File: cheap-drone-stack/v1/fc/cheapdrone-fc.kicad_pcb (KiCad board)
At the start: 4 copper layers, 33.8 x 33.8 mm, 77 parts, among them Y1 8MHz

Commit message: Cheap drone stack: OffGrid brand silkscreen on the FC, verification script
- brand.py: Beacon Ring and lockup from the v3.2 hand-off SVG numbers,
  Instrument Sans / JetBrains Mono outlines shaped with HarfBuzz from the
  vendored OFL variable fonts; styles follow tokens.json
- FC: lockup on the bottom, bare mark and pad codes on the top, matte black
  mask / white silk / ENIG written into the board stackup; LED and spare
  GND breakout pads swapped so every label fits at a printable size
- ESC: six layers (In1 GND, In4 VBAT, four signal layers); bottom channels
  trade MCU and BEMF ends so no two QFNs sit back to back (routing WIP)
- verify.py: pin maps against KiCad symbols and the Betaflight/AM32
  sources, power arithmetic, DRC/netlist/fab checks, silkscreen stroke
  widths, brand mark against the brand PNG

Co-Authored-By: Claude Opus 5.5 <noreply@anthropic.com>
Claude-Session: https://claude.ai/code/session_01MaVFAzoExts7u2gmCraXFC
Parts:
- moved P_G1 4.20 mm to (84.2, 105.8)
- moved P_LED 4.20 mm to (84.2, 110.0)
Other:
- board text removed: "1"
- board text removed: "3V3"
- board text removed: "5V"
- board text removed: "BOOT"
- board text removed: "BZ+"
- board text removed: "BZ-"
- board text removed: "Betaflight CHEAPDRONE_G473"
- board text removed: "CLK"
- board text removed: "DIO"
- board text removed: "ESC"
- board text removed: "ESC lead 1 VBAT 2 GND 3 CUR 4 TLM 5-8 M1-M4"
- board text removed: "FRONT"
- board text removed: "G"
- board text removed: "LED"
- board text removed: "OFFGRID CHEAP DRONE FC v1"
- board text removed: "R1"
- board text removed: "R2"
- board text removed: "R4"
- board text removed: "RST"
- board text removed: "STM32G473 ICM-42688-P 16MB"
- board text removed: "T1"
- board text removed: "T2"
- board text removed: "T4"
- board text removed: "VB"

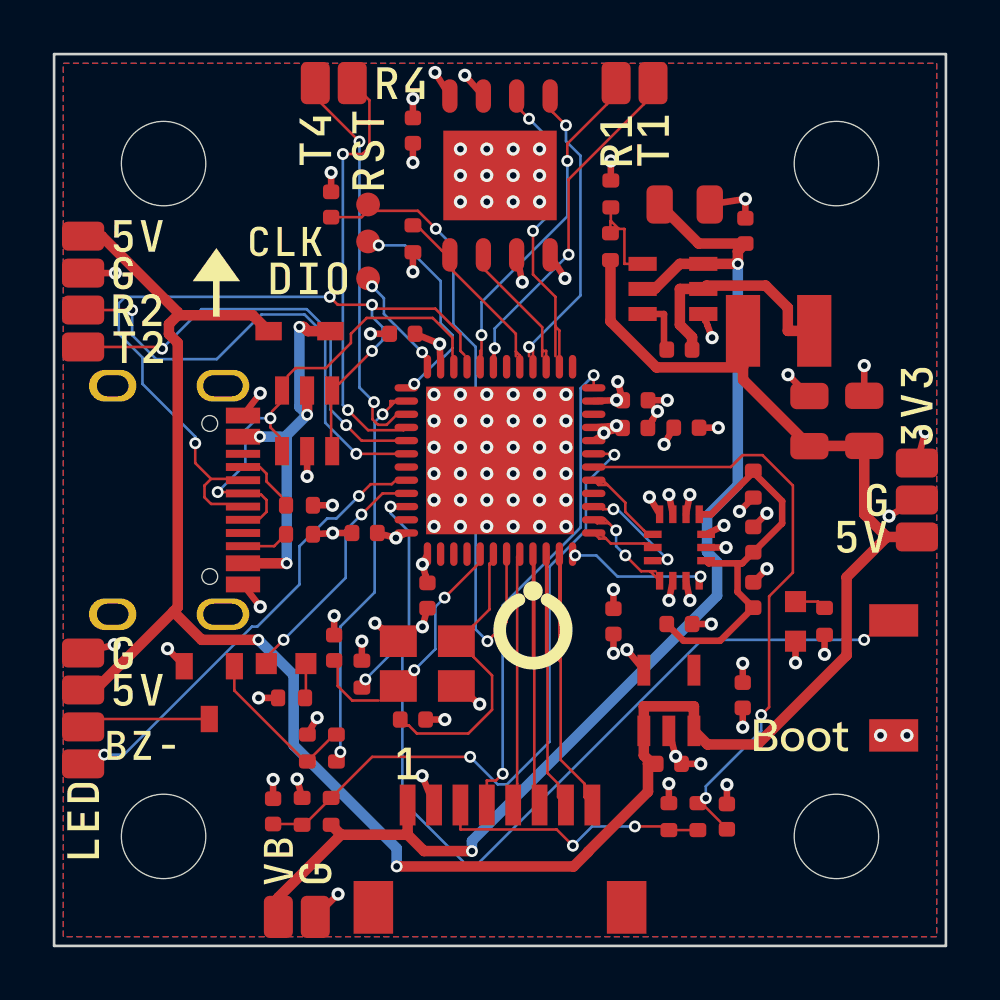
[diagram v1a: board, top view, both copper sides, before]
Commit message: Review fixes: 5 A BEC inductor, BMI270/Puya second sources, ESC gate clamp
From the independent design review and the bulk-sourcing audit:
- FC BEC inductor FNR3015 (Isat 1.4 A) -> FXL0530 (Isat 5 A, above the
  LMR51420 current limit); corner re-placed and re-routed, DRC 0/0/0
- IMU pins 2/3 opened so the pads take a BMI270 (BOM default, $1.36, in
  stock) or the ICM-42688-P; flash -> Puya PY25Q128HA on the same land;
  CPL carries a per-part rotation for footprints JLCPCB draws turned round
- beeper FET 2N7002 -> AO3400A (specified at 2.5 V gate drive); blue LED
  resistor 1k -> 330R
- ESC: driver VCC through 330R with a 15 V Zener per channel (gates 5 V
  inside the FETs' 20 V rating); 4.7 uF at each MCU; Samsung 10 uF caps
- motor poles 14 -> 12 (XING2 1404 is 9N12P)

Co-Authored-By: Claude Opus 5.5 <noreply@anthropic.com>
Claude-Session: https://claude.ai/code/session_01MaVFAzoExts7u2gmCraXFC
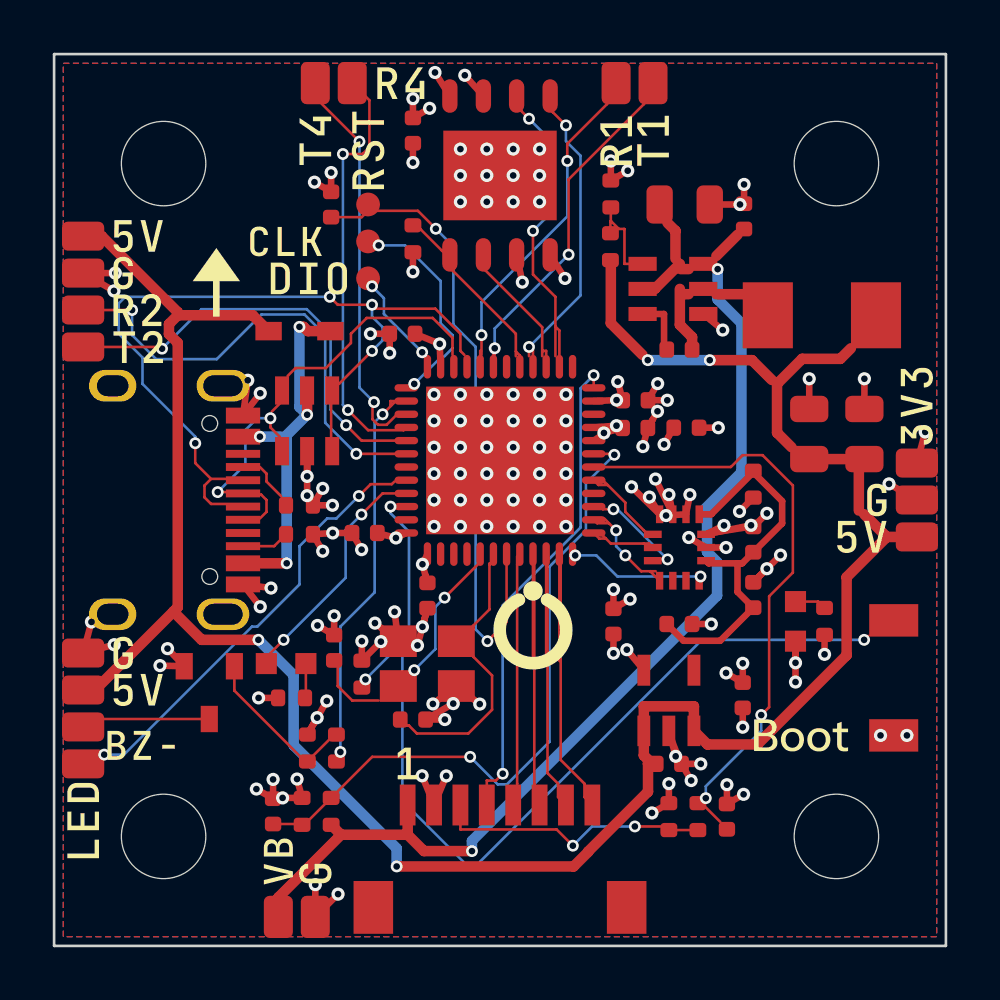
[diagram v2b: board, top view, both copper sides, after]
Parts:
- L1: footprint IND-SMD_L3.0-W3.0_FNR30XXS -> aio:IND-SMD_L5.4-W5.2_FXL0530
- moved L1 1.74 mm to (112.2, 93.0)
- moved C4 0.55 mm to (109.2, 89.2)
- moved C7 0.50 mm to (113.8, 97.5)
- moved C6 0.49 mm to (111.7, 97.5)
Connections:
- U_IMU pad 2: GND -> (no net)
- U_IMU pad 3: GND -> (no net)
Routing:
- net GND: track 46.9 -> 86.9 mm, vias 97 -> 134
- net BUCK_SW: track 8.86 -> 3.64 mm
- net VBAT: track 46.5 -> 42.6 mm
- net +5V: track 89.4 -> 88.2 mm, vias 2 -> 4
